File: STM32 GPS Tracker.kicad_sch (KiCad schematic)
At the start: 15 parts, among them J1 693010020611, Q1 AO3407A, U1 STM32F030C8Tx, U2 SIM808, U3 SMF05CT1G, U4 TPS5430DDA

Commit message: Placing and wiring components for Voltage regulation ckt in Schematic
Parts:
- added C6: 4u7, symbol Device:C
- added C7: 10n, symbol Device:C
- added D2: B340, Diode_SMD:D_SMC, symbol Diode:B340
- added F1: Fuse 2.5A, symbol Device:Fuse
- C4: value C -> 10u
- renumbered J1 to J3, U2 to U1, U4 to U2, U1 to U4
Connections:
- net GND: now also C4.2, Q1.1 (G), U2.6 (GND), U2.9 (EP), D2.2 (A)
- net at U2.1 (BOOT): now also C7.2
- net FEEDBACK: now reaches U2.4 (VSENSE)
- net at U2.7 (VIN): now also Q1.2 (S)
- net at U2.8 (PH): now also C7.1, D2.1 (K)
- net at Q1.3 (D): now also C4.1, F1.2
- new net +12V: F1.1
- no-connect marks 35 -> 36
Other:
- moved on the sheet: C4, Q1

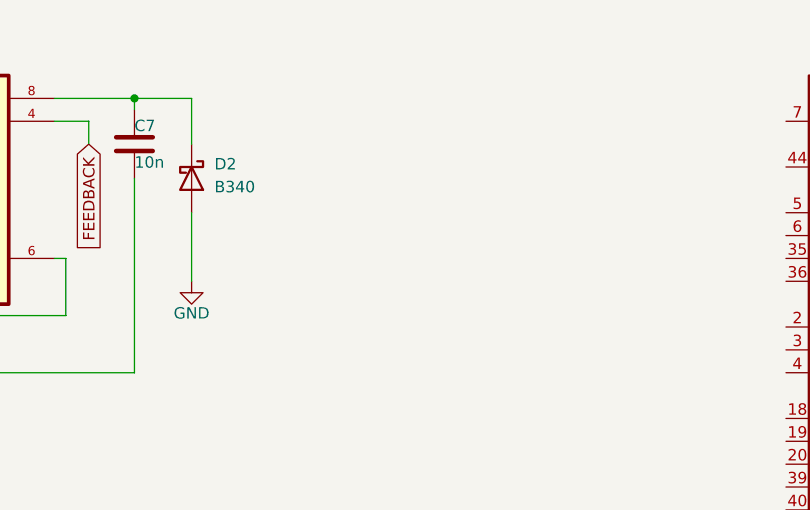
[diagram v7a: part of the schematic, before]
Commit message: remaining Placing and wiring components for Voltage regulation ckt in Schematic
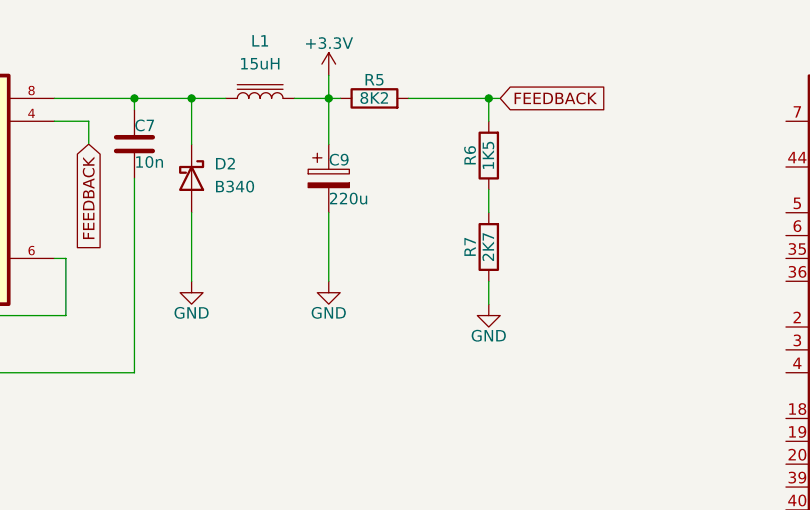
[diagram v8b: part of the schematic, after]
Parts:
- added C9: 220u, symbol Device:C_Polarized
- added L1: 15uH, symbol Device:L_Iron
- added R5: 8K2, symbol Device:R
- added R6: 1K5, symbol Device:R
- added R7: 2K7, symbol Device:R
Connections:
- net +3.3V: now also C9.1, L1.2, R5.1
- net FEEDBACK: now also R5.2, R6.2
- net GND: now also C9.2, R7.1
- net at C7.1, D2.1 (K), U2.8 (PH): now also L1.1
- new net: R6.1, R7.2
